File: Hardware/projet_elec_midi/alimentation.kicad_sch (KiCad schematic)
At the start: 11 parts, among them J1 BATTERY, J5 USB_C_Receptacle_USB2.0_16P, U2 MCP73811T-420I-OT, U3 USBLC6-2SC6, U8 MCP1802x-xx02xOT

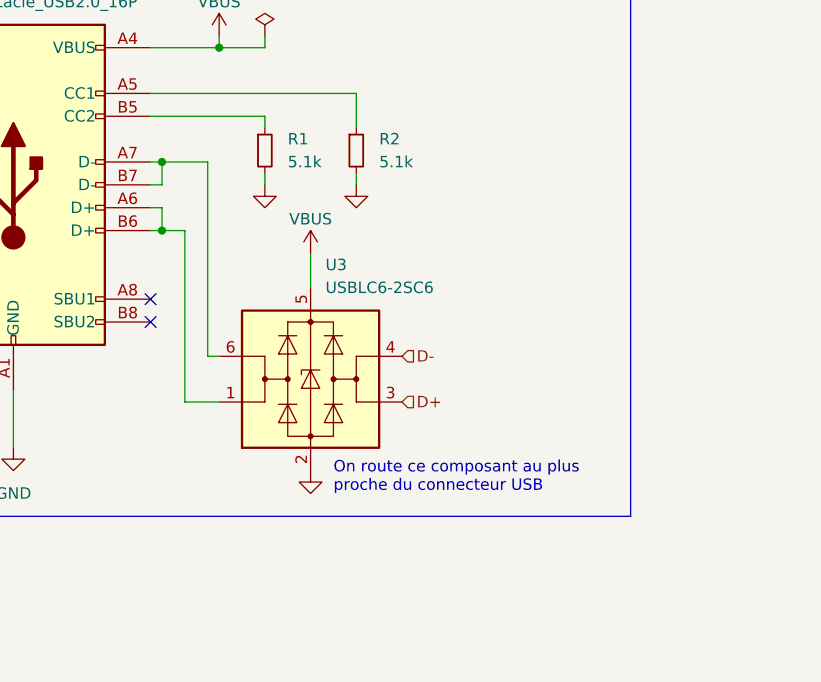
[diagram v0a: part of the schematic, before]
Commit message: Routage en double face
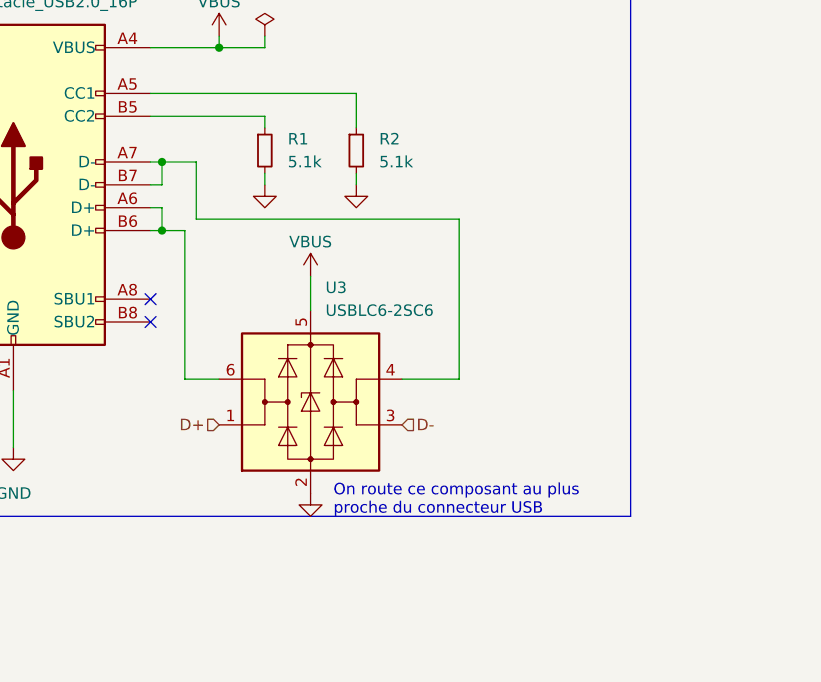
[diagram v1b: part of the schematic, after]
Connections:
- net D+: now also U3.1 (I/O1); no longer U3.3 (I/O2)
- net D-: now also U3.3 (I/O2); no longer U3.4 (I/O2)
- net at J5.A6 (D+), J5.B6 (D+): now also U3.6 (I/O1); no longer U3.1 (I/O1)
- net at J5.A7 (D-), J5.B7 (D-): now also U3.4 (I/O2); no longer U3.6 (I/O1)
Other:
- moved on the sheet: U3
